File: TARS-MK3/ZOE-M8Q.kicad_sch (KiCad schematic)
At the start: 5 parts, among them U8001 ZOE-M8Q, X8001 SMACONNECTOR

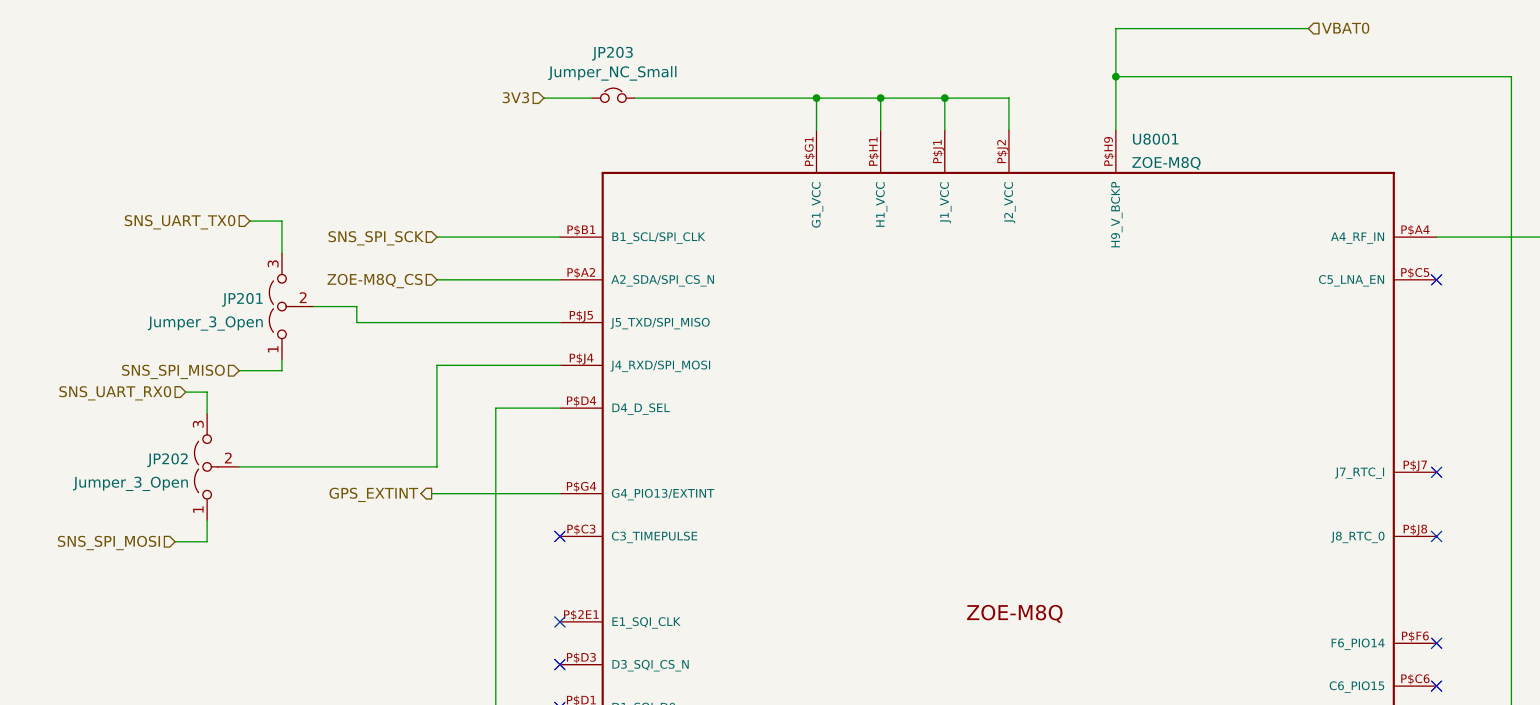
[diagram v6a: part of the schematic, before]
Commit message: Completed sensor suite and added uFL connector
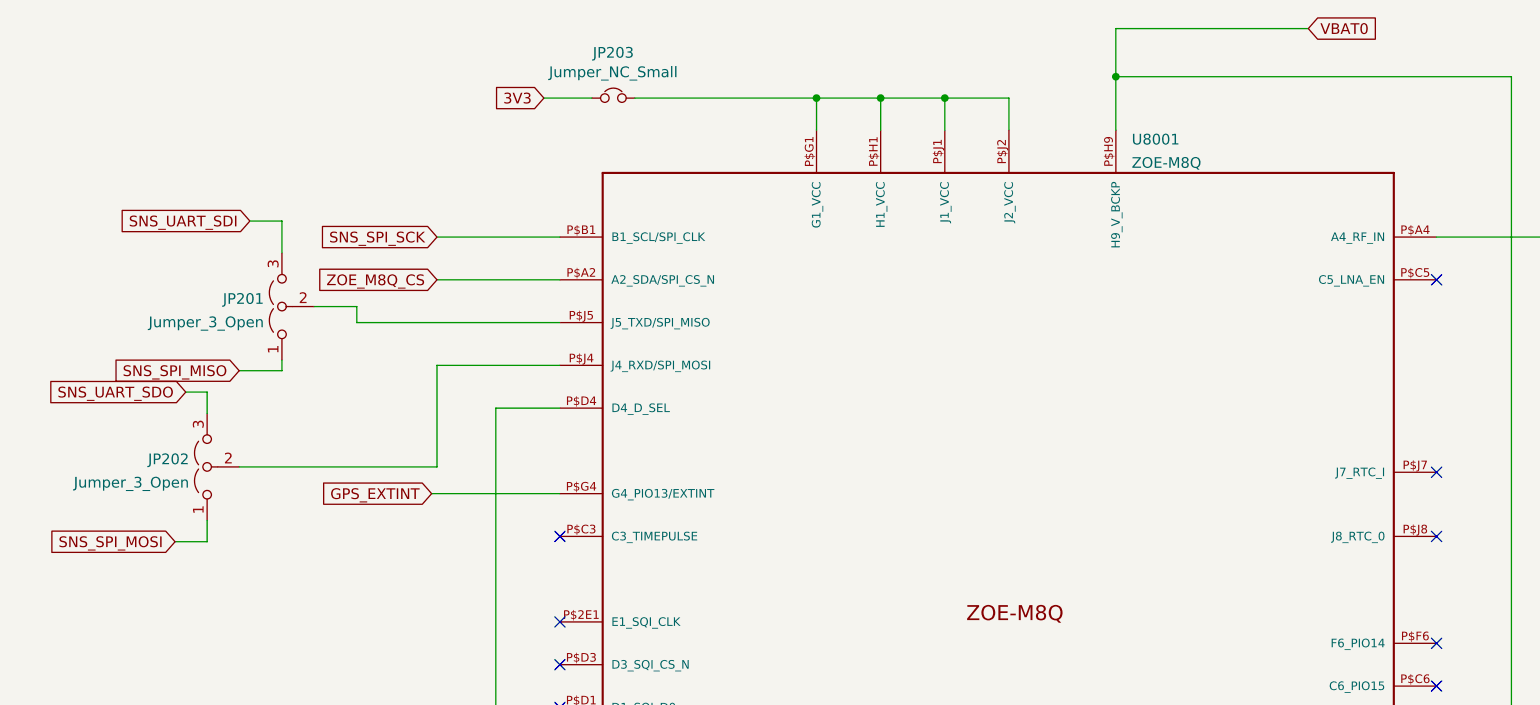
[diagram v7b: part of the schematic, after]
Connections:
- net SNS_UART_RX0 renamed SNS_UART_SDO
- net SNS_UART_TX0 renamed SNS_UART_SDI
- net ZOE-M8Q_CS renamed ZOE_M8Q_CS
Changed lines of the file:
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@@
     (stroke (width 0) (type default) (color 0 0 0 0))
   )
-  (hierarchical_label "ZOE-M8Q_CS" (shape input) (at 56.515 53.975 180)
+  (global_label "SNS_SPI_SCK" (shape input) (at 56.515 48.895 180) (fields_autoplaced)
     (effects (font (size 1.27 1.27)) (justify right))
+    (property "Intersheet References" "${INTERSHEET_REFS}" (id 0) (at 41.6722 48.8156 0)
+      (effects (font (size 1.27 1.27)) (justify right) hide)
+    )
   )
-  (hierarchical_label "GPS_EXTINT" (shape output) (at 55.88 79.375 180)
+  (global_label "SNS_SPI_MOSI" (shape input) (at 25.4 85.09 180) (fields_autoplaced)
     (effects (font (size 1.27 1.27)) (justify right))
+    (property "Intersheet References" "${INTERSHEET_REFS}" (id 0) (at 9.7106 85.0106 0)
+      (effects (font (size 1.27 1.27)) (justify right) hide)
+    )
   )
-  (hierarchical_label "VBAT0" (shape input) (at 160.02 24.13 0)
+  (global_label "SNS_UART_SDO" (shape input) (at 26.67 67.31 180) (fields_autoplaced)
+    (effects (font (size 1.27 1.27)) (justify right))
+    (property "Intersheet References" "${INTERSHEET_REFS}" (id 0) (at 10.1944 67.2306 0)
+      (effects (font (size 1.27 1.27)) (justify right) hide)
+    )
+  )
+  (global_label "SNS_SPI_MISO" (shape input) (at 33.02 64.77 180) (fields_autoplaced)
+    (effects (font (size 1.27 1.27)) (justify right))
+    (property "Intersheet References" "${INTERSHEET_REFS}" (id 0) (at 17.3306 64.6906 0)
+      (effects (font (size 1.27 1.27)) (justify right) hide)
+    )
+  )
+  (global_label "3V3" (shape input) (at 69.215 32.385 180) (fields_autoplaced)
+    (effects (font (size 1.27 1.27)) (justify right))
+    (property "Intersheet References" "${INTERSHEET_REFS}" (id 0) (at 63.3832 32.3056 0)
+      (effects (font (size 1.27 1.27)) (justify right) hide)
+    )
+  )
+  (global_label "ZOE_M8Q_CS" (shape input) (at 56.515 53.975 180) (fields_autoplaced)
+    (effects (font (size 1.27 1.27)) (justify right))
+    (property "Intersheet References" "${INTERSHEET_REFS}" (id 0) (at 42.0956 53.8956 0)
+      (effects (font (size 1.27 1.27)) (justify right) hide)
+    )
+  )
+  (global_label "SNS_UART_SDI" (shape input) (at 34.29 46.99 180) (fields_autoplaced)
+    (effects (font (size 1.27 1.27)) (justify right))
+    (property "Intersheet References" "${INTERSHEET_REFS}" (id 0) (at 18.5401 46.9106 0)
+      (effects (font (size 1.27 1.27)) (justify right) hide)
+    )
+  )
+  (global_label "VBAT0" (shape input) (at 160.02 24.13 0) (fields_autoplaced)
     (effects (font (size 1.27 1.27)) (justify left))
+    (property "Intersheet References" "${INTERSHEET_REFS}" (id 0) (at 167.9685 24.0506 0)
+      (effects (font (size 1.27 1.27)) (justify left) hide)
+    )
   )
-  (hierarchical_label "3V3" (shape input) (at 69.215 32.385 180)
+  (global_label "GPS_EXTINT" (shape input) (at 55.88 79.375 180) (fields_autoplaced)
     (effects (font (size 1.27 1.27)) (justify right))
-  )
-  (hierarchical_label "SNS_SPI_MISO" (shape input) (at 33.02 64.77 180)
-    (effects (font (size 1.27 1.27)) (justify right))
-  )
-  (hierarchical_label "SNS_UART_TX0" (shape input) (at 34.29 46.99 180)
-    (effects (font (size 1.27 1.27)) (justify right))
-  )
-  (hierarchical_label "SNS_SPI_MOSI" (shape input) (at 25.4 85.09 180)
-    (effects (font (size 1.27 1.27)) (justify right))
-  )
-  (hierarchical_label "SNS_SPI_SCK" (shape input) (at 56.515 48.895 180)
-    (effects (font (size 1.27 1.27)) (justify right))
-  )
-  (hierarchical_label "SNS_UART_RX0" (shape input) (at 26.67 67.31 180)
-    (effects (font (size 1.27 1.27)) (justify right))
+    (property "Intersheet References" "${INTERSHEET_REFS}" (id 0) (at 42.6096 79.2956 0)
+      (effects (font (size 1.27 1.27)) (justify right) hide)
+    )
   )
   (symbol (lib_id "Device:Jumper_NC_Small") (at 77.47 32.385 0) (unit 1)

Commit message: PMB fixups
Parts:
- added JP204: Jumper_NC_Small, Jumper:SolderJumper-2_P1.3mm_Bridged_RoundedPad1.0x1.5mm, symbol Device:Jumper_NC_Small
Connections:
- net GND: now also JP204.1; no longer U8001.P$D4 (D4_D_SEL)
- new net: JP204.2, U8001.P$D4 (D4_D_SEL)
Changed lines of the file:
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@@
   (junction (at 91.44 168.275) (diameter 0) (color 0 0 0 0)
   )
+  (junction (at 63.5 168.275) (diameter 0) (color 0 0 0 0)
+  )
   (junction (at 142.24 168.275) (diameter 0) (color 0 0 0 0)
   )
   (junction (at 137.16 168.275) (diameter 0) (color 0 0 0 0)
+  )
+  (junction (at 71.12 69.215) (diameter 0) (color 0 0 0 0)
   )
   (junction (at 157.48 168.275) (diameter 0) (color 0 0 0 0)
@@
     (stroke (width 0) (type default) (color 0 0 0 0))
   )
+  (wire (pts (xy 63.5 168.275) (xy 63.5 168.91))
+    (stroke (width 0) (type default) (color 0 0 0 0))
+  )
   (wire (pts (xy 162.56 160.655) (xy 162.56 168.275))
     (stroke (width 0) (type default) (color 0 0 0 0))
@@
     (stroke (width 0) (type default) (color 0 0 0 0))
   )
+  (wire (pts (xy 63.5 69.85) (xy 63.5 168.275))
+    (stroke (width 0) (type default) (color 0 0 0 0))
+  )
   (wire (pts (xy 201.295 41.275) (xy 203.835 41.275))
     (stroke (width 0) (type default) (color 0 0 0 0))
@@
     (stroke (width 0) (type default) (color 0 0 0 0))
   )
+  (wire (pts (xy 71.12 69.215) (xy 71.12 69.85))
+    (stroke (width 0) (type default) (color 0 0 0 0))
+  )
   (wire (pts (xy 86.36 160.655) (xy 86.36 168.275))
     (stroke (width 0) (type default) (color 0 0 0 0))
@@
     (stroke (width 0) (type default) (color 0 0 0 0))
   )
-  (wire (pts (xy 63.5 69.215) (xy 63.5 168.275))
-    (stroke (width 0) (type default) (color 0 0 0 0))
-  )
   (wire (pts (xy 101.6 160.655) (xy 101.6 168.275))
     (stroke (width 0) (type default) (color 0 0 0 0))
@@
     (stroke (width 0) (type default) (color 0 0 0 0))
   )
-  (wire (pts (xy 71.12 69.215) (xy 63.5 69.215))
-    (stroke (width 0) (type default) (color 0 0 0 0))
-  )
   (wire (pts (xy 26.67 67.31) (xy 29.21 67.31))
     (stroke (width 0) (type default) (color 0 0 0 0))
@@
     (stroke (width 0) (type default) (color 0 0 0 0))
   )
+  (wire (pts (xy 68.58 69.85) (xy 71.12 69.85))
+    (stroke (width 0) (type default) (color 0 0 0 0))
+  )
   (wire (pts (xy 147.32 160.655) (xy 147.32 168.275))
+    (stroke (width 0) (type default) (color 0 0 0 0))
+  )
+  (wire (pts (xy 71.12 68.58) (xy 71.12 69.215))
     (stroke (width 0) (type default) (color 0 0 0 0))
   )
@@
     (pin "3")
   )
+  (symbol (lib_id "Device:Jumper_NC_Small") (at 66.04 69.85 0) (unit 1)
+    (in_bom yes) (on_board yes)
+    (property "Reference" "JP204" (id 0) (at 66.04 64.4652 0))
+    (property "Value" "Jumper_NC_Small" (id 1) (at 66.04 66.7766 0))
+    (property "Footprint" "Jumper:SolderJumper-2_P1.3mm_Bridged_RoundedPad1.0x1.5mm" (id 2) (at 66.04 69.85 0)
+      (effects (font (size 1.27 1.27)) hide)
+    )
+    (property "Datasheet" "~" (id 3) (at 66.04 69.85 0)
+      (effects (font (size 1.27 1.27)) hide)
+    )
+    (pin "1")
+    (pin "2")
+  )
   (symbol (lib_id "ZOE-M8Q:ZOE-M8Q") (at 147.32 130.175 0) (unit 1)
